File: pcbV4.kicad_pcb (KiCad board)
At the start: 4 copper layers, 61.1 x 30 mm, 55 parts, among them J3 GND, J4 GND, J5 VDD, J6 SWDCLK, J7 SWDIO, SW1 XDMK-12C01-25, U1 LSM6DSOXTR, U2 MAX30001CWV+T, U4 NPM1100-QDAA-R, U5 BS-08-B2AA020-R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

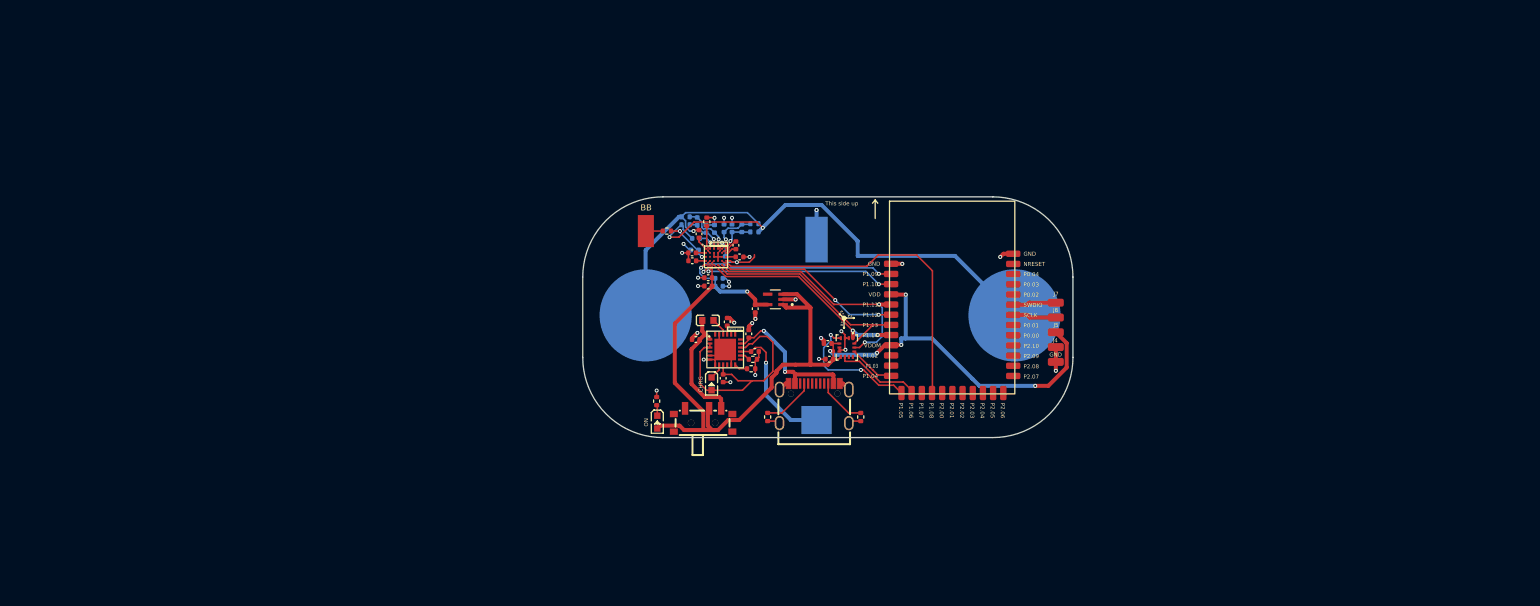
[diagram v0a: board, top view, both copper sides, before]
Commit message: Update pcbV4 KiCad design
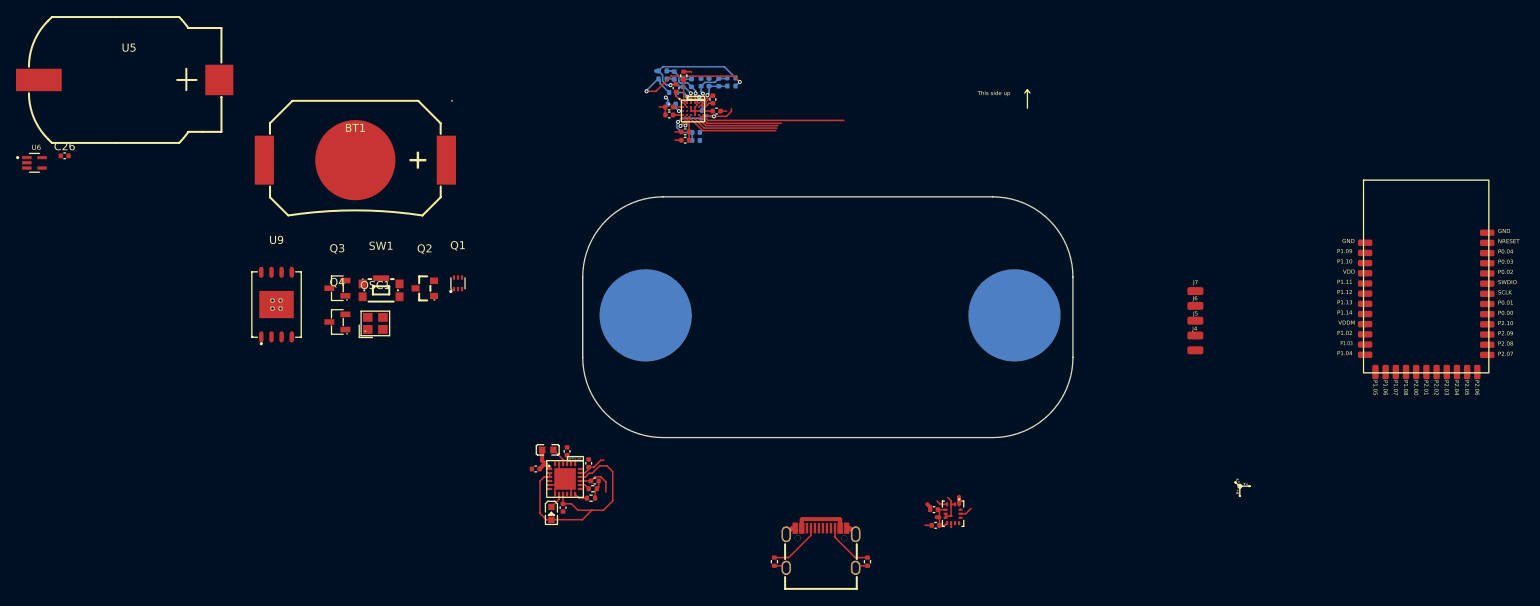
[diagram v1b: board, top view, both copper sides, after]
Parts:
- removed BB: Conn_01x01_Pin, Connector_Wire:SolderWirePad_1x01_SMD_5x10mm
- removed LED2: Blue light 0603, easyeda2kicad:LED0603-RD
- removed R11: 4k7, Resistor_SMD:R_0402_1005Metric
- removed R5: 200k, Resistor_SMD:R_0402_1005Metric
- added BT1: MY-2032-12, easyeda2kicad:BAT-SMD_MY-2032-12, F.Cu at (71.4, 81.6)
- added OSC1: SX2M32.768KM20F30TNN, easyeda2kicad:OSC-SMD_4P-L2.5-W2.0-BL, F.Cu at (73.9, 101.9)
- added Q1: DMC2400UV-7, easyeda2kicad:SOT-563_L1.6-W1.2-P0.50-LS1.6-BL, F.Cu at (84.2, 96.9)
- added Q2: AO3401A, easyeda2kicad:SOT-23_L2.9-W1.3-P1.90-LS2.4-BR, F.Cu at (80.0, 97.6)
- added Q3: MMBT3904-TP, easyeda2kicad:SOT-23-3_L2.9-W1.3-P1.90-LS2.4-BR, F.Cu at (69.1, 97.6)
- added Q4: MMBT3904-TP, easyeda2kicad:SOT-23-3_L2.9-W1.3-P1.90-LS2.4-BR, F.Cu at (69.1, 101.8)
- added U9: W25Q256JVEIQTR, easyeda2kicad:WSON-8_L8.0-W6.10-P1.27-BL-EP, F.Cu at (61.5, 99.6)
- C13: value C -> 10uF
- J3: value GND -> NRESET
- R3, R4: value 200k -> 200
- R9: value 1k5 -> 14k
- SW1: value XDMK-12C01-25 -> KMR221GLFS; footprint easyeda2kicad:SW-SMD_XDMK-12C01-25 -> easyeda2kicad:KEY-SMD_KMR2XXGXXX
- U5: moved to F.Cu
- moved U6 94.0 mm to (31.3, 81.9), turned to 0 degrees
- moved U5 91.2 mm to (43.1, 71.6), turned to 0 degrees
- moved C26 88.2 mm to (35.1, 81.0), turned to 0 degrees
- moved U3 59.2 mm to (197.1, 84.1)
- moved SW1 43.4 mm to (74.6, 97.5), turned to 0 degrees
- moved C21 25.7 mm to (93.9, 120.1)
- moved C22 25.7 mm to (100.5, 119.4)
- moved C24 25.7 mm to (101.2, 121.6)
- moved C23 25.7 mm to (97.8, 117.9)
- moved C25 25.7 mm to (97.3, 124.9)
- moved L1 25.7 mm to (95.4, 117.7)
- moved LED1 25.7 mm to (95.8, 125.6)
- moved R10 25.7 mm to (101.0, 122.6)
- moved R9 25.7 mm to (100.8, 123.7)
- moved U4 25.7 mm to (97.5, 121.3)
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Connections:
- C1 pad 2: bat- -> GND
- C10 pad 2: bat- -> GND
- C12 pad 2: bat- -> GND
- C13 pad 2: bat- -> GND
- C14 pad 2: bat- -> GND
- C15 pad 2: bat- -> GND
- C16 pad 2: bat- -> GND
- C17 pad 2: bat- -> GND
- C18 pad 2: bat- -> GND
- C19 pad 2: bat- -> GND
- C20 pad 2: bat- -> GND
- C21 pad 1: VOUT -> npm_out
- C21 pad 2: bat- -> GND
- C22 pad 1: bat- -> GND
- C23 pad 2: bat- -> GND
- C24 pad 2: bat- -> GND
- C25 pad 2: bat- -> GND
- C26 pad 2: bat- -> GND
- C4 pad 2: bat- -> GND
- C5 pad 1: bat- -> GND
- C6 pad 2: bat- -> GND
- C7 pad 1: bat- -> GND
- J3 pad 1: bat- -> NRESET
- J4 pad 1: bat- -> GND
- L1 pad 1: VOUT -> npm_out
- R10 pad 1: bat- -> GND
- R6 pad 2: bat- -> GND
- R7 pad 2: bat- -> GND
- R8 pad 2: bat- -> GND
- R9 pad 1: bat- -> GND
- SW1 pad 1: VOUT -> Net-(Q3-B)
- SW1 pad 2: VDD -> unconnected-(SW1-Pad2)
- SW1 pad 3: unconnected-(SW1-Pad3) -> Net-(Q4-C)
- SW1 pad 4: (no net) -> unconnected-(SW1-Pad4)
- SW1 pad 5: (no net) -> unconnected-(SW1-Pad5)
- U1 pad 2: bat- -> GND
- U1 pad 3: bat- -> GND
- U1 pad 6: bat- -> GND
- U1 pad 7: bat- -> GND
- U2 pad B3: bat- -> GND
- U2 pad B4: bat- -> GND
- U2 pad C3: bat- -> GND
- U2 pad C4: bat- -> GND
- U2 pad C5: bat- -> GND
- U2 pad D4: bat- -> GND
- U3 pad 1: bat- -> GND
- U3 pad 16: FCLK -> unconnected-(U3-P1.08-Pad16)
- U3 pad 36: bat- -> GND
- U4 pad 1: VOUT -> npm_out
- U4 pad 11: bat- -> GND
- U4 pad 23: bat- -> GND
- U4 pad 25: bat- -> GND
- U4 pad 5: bat- -> GND
- U4 pad 6: bat- -> SHPACT
- U4 pad 7: bat- -> GND
- U5 pad 2: bat- -> GND
- U6 pad 2: bat- -> GND
- USBC1 pad 1: bat- -> GND
- USBC1 pad 2: bat- -> GND
- USBC1 pad 3: bat- -> GND
- USBC1 pad 4: bat- -> GND
- USBC1 pad A1B12: bat- -> GND
- USBC1 pad B1A12: bat- -> GND
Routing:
- net VDD: track 120.9 -> 7.89 mm, vias 5 -> 0
- net bat-: track 60.3 -> 0.00 mm, vias 28 -> 0
- net ECGN: track 58.0 -> 17.9 mm
- net GND: track 0.00 -> 36.3 mm, vias 0 -> 2
- net FCLK: track 43.2 -> 18.3 mm
- net INT2B_MAX30001: track 24.4 -> 0.90 mm, vias 2 -> 1
- net INTB_MAX30001: track 25.7 -> 2.92 mm, vias 2 -> 1
- net SCLK: track 31.4 -> 11.8 mm, vias 2 -> 0
- net MOSI: track 28.3 -> 10.7 mm
- net INT1_LSM: track 16.7 -> 1.42 mm, vias 2 -> 0
- net VOUT: track 15.3 -> 0.00 mm
- net MISO: track 26.7 -> 12.1 mm, vias 2 -> 0
- net ECGP: track 28.1 -> 14.1 mm
- net CS_MAX: track 23.2 -> 9.98 mm, vias 2 -> 0
- net bat+: track 16.6 -> 4.92 mm, vias 1 -> 0
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- added copper zone on In1.Cu, net GND
- added copper zone on In2.Cu, net GND
- removed copper zone on In1.Cu, net bat-
- removed copper zone on In2.Cu, net bat-
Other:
- board text removed: "CHRG"
- board text removed: "ON"

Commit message: Update pcbV4 KiCad design
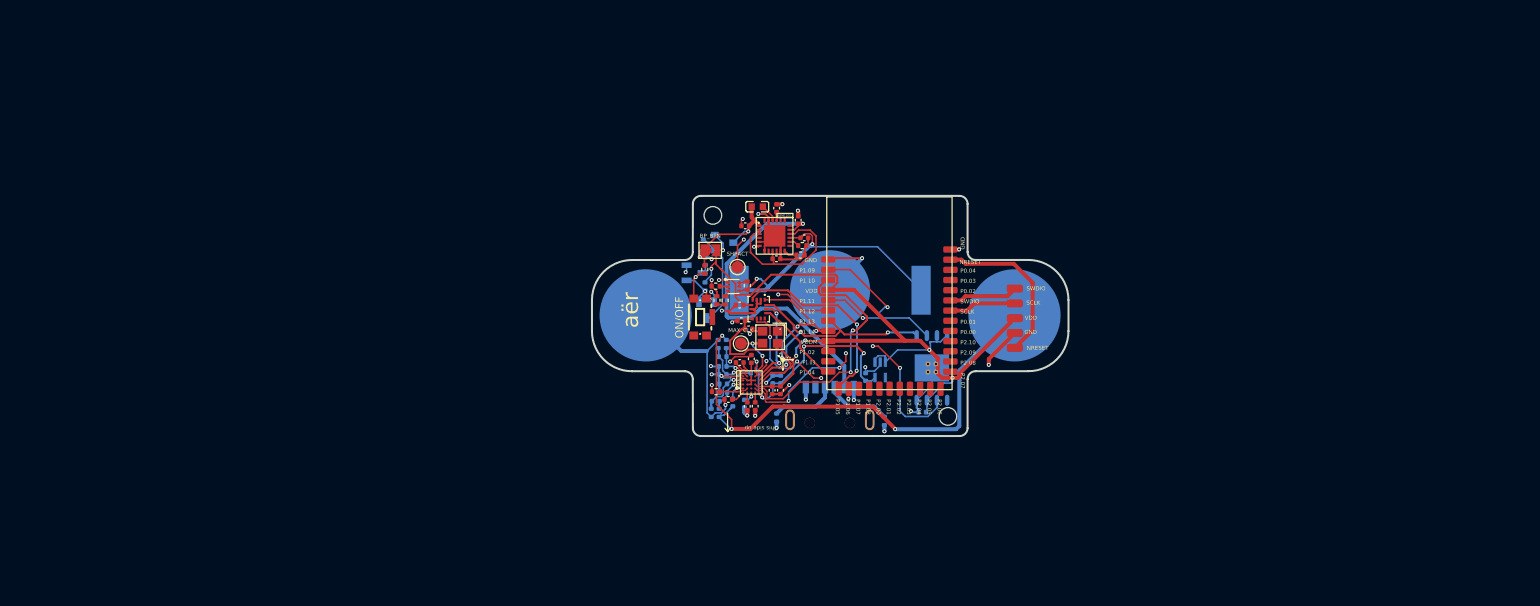
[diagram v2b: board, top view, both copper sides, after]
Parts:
- removed LED1: Blue light 0603, easyeda2kicad:LED0603-RD
- removed SW1: KMR221GLFS, easyeda2kicad:KEY-SMD_KMR2XXGXXX
- removed U5: BS-08-B2AA020-R, easyeda2kicad:BAT-SMD_BS-08-B2AA016
- removed USBC1: TYPE-C-31-M-12, easyeda2kicad:USB-C_SMD-TYPE-C-31-M-12_1
- added BP_BTN: SolderJumper_2_Open, Jumper:SolderJumper-2_P1.3mm_Open_TrianglePad1.0x1.5mm, F.Cu at (115.6, 92.8)
- added C28: 0.01uF, Capacitor_SMD:C_0402_1005Metric, F.Cu at (120.4, 102.6)
- added C29: 22uF, Capacitor_SMD:C_0402_1005Metric, B.Cu at (115.0, 94.2)
- added C30: 100nF, Capacitor_SMD:C_0402_1005Metric, B.Cu at (142.1, 113.0)
- added H1: MountingHole, MountingHole:MountingHole_2.2mm_M2, F.Cu at (145.3, 113.5)
- added H2: MountingHole, MountingHole:MountingHole_2.2mm_M2, F.Cu at (116.0, 88.5)
- added MAX_CLK: TestPoint, TestPoint:TestPoint_Pad_D1.5mm, F.Cu at (119.5, 104.5)
- added ON/OFF: KMR221GLFS, easyeda2kicad:KEY-SMD_KMR2XXGXXX, F.Cu at (114.7, 101.2)
- added R11: 1M, Resistor_SMD:R_0402_1005Metric, F.Cu at (116.3, 97.3)
- added R12: 1M5, Resistor_SMD:R_0402_1005Metric, F.Cu at (117.5, 99.1)
- added R13: 220k, Resistor_SMD:R_0402_1005Metric, F.Cu at (116.5, 99.1)
- added R14: 1M, Resistor_SMD:R_0402_1005Metric, F.Cu at (120.2, 97.2)
- added R15: 100k, Resistor_SMD:R_0402_1005Metric, B.Cu at (114.8, 92.0)
- added R16: 100k, Resistor_SMD:R_0402_1005Metric, B.Cu at (115.0, 97.3)
- added R17: 660k, Resistor_SMD:R_0402_1005Metric, F.Cu at (114.9, 95.2)
- added SHPACT: TestPoint, TestPoint:TestPoint_Pad_D1.5mm, F.Cu at (119.0, 94.9)
- added USB2: USBC-0032IPX8-00, easyeda2kicad:TYPE-C-USB-SMD_USBC-0032IPX8-00, B.Cu at (130.5, 111.9)
- BT1, C26, Q2, Q3, Q4, R7, R8, U6, U9: moved to B.Cu
- moved U6 108.6 mm to (136.8, 107.7), turned to -90 degrees
- moved C26 103.6 mm to (135.0, 108.6), turned to 90 degrees
- moved U9 82.1 mm to (143.3, 107.5), turned to 180 degrees
- moved U3 67.0 mm to (130.2, 86.2)
- moved BT1 61.4 mm to (130.6, 97.8)
- moved OSC1 49.3 mm to (123.1, 103.7), turned to 180 degrees
- moved Q3 46.1 mm to (115.2, 100.3), turned to 90 degrees
- moved Q4 45.0 mm to (113.7, 95.6), turned to 180 degrees
- moved R3 43.1 mm to (115.7, 113.1), turned to 90 degrees
- moved R4 42.2 mm to (116.7, 113.1), turned to 90 degrees
- moved C3 41.0 mm to (116.3, 111.6), turned to 0 degrees
- moved C25 40.9 mm to (123.9, 93.9), turned to 0 degrees
- moved C21 40.0 mm to (120.0, 89.8)
- moved C22 40.0 mm to (126.6, 89.1)
- moved C24 40.0 mm to (127.4, 91.3)
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- renumbered J4 to GND, J6 to SCLK, J7 to SWDIO, J5 to VDD
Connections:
- R7 pad 1: Net-(USBC1-CC2) -> GND
- R7 pad 2: GND -> Net-(USB2-CC1)
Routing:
- net VDD: track 7.89 -> 122.7 mm, vias 0 -> 6
- net GND: track 36.3 -> 108.3 mm, vias 2 -> 30
- net ECGN: track 17.9 -> 65.9 mm, vias 2 -> 3
- net MISO: track 12.1 -> 48.5 mm, vias 0 -> 5
- net bat+: track 4.92 -> 37.2 mm, vias 0 -> 2
- net INTB_MAX30001: track 2.92 -> 34.8 mm, vias 1 -> 4
- net VBUS: track 10.7 -> 41.2 mm, vias 0 -> 1
- net INT2B_MAX30001: track 0.90 -> 31.3 mm, vias 1 -> 2
- net SCLK: track 11.8 -> 36.1 mm, vias 0 -> 3
- net INT1_LSM: track 1.42 -> 24.6 mm, vias 0 -> 2
- net MOSI: track 10.7 -> 32.4 mm, vias 0 -> 3
- net NRESET: track 0.00 -> 20.5 mm
- net INT2_LSM: track 0.57 -> 20.2 mm, vias 0 -> 4
- net VCC: track 13.4 -> 29.9 mm, vias 2 -> 4
- net npm_out: track 3.68 -> 18.2 mm, vias 0 -> 2
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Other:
- board size 61.1 x 30 mm -> 59.4 x 30 mm
- board text added: "aër"

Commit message: Update pcbV4 KiCad design
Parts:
- removed BP_BTN: SolderJumper_2_Open, Jumper:SolderJumper-2_P1.3mm_Open_TrianglePad1.0x1.5mm
- removed C28: 0.01uF, Capacitor_SMD:C_0402_1005Metric
- removed C29: 22uF, Capacitor_SMD:C_0402_1005Metric
- removed OSC1: SX2M32.768KM20F30TNN, easyeda2kicad:OSC-SMD_4P-L2.5-W2.0-BL
- removed Q2: AO3401A, easyeda2kicad:SOT-23_L2.9-W1.3-P1.90-LS2.4-BR
- removed Q3, Q4: MMBT3904-TP, easyeda2kicad:SOT-23-3_L2.9-W1.3-P1.90-LS2.4-BR
- removed R15, R16: 100k, Resistor_SMD:R_0402_1005Metric
- removed R17: 660k, Resistor_SMD:R_0402_1005Metric
- added G***: LOGO, easyeda2kicad:aer_logo, F.Cu at (107.2, 101.2)
- added LED1: 19-237/R6GHBHC-A07/2T, easyeda2kicad:LED-ARRAY-SMD_4P-L1.6-W1.6-BL-CW, F.Cu at (125.8, 96.3)
- added MISO: TestPoint, TestPoint:TestPoint_Pad_D1.5mm, F.Cu at (138.6, 112.8)
- added MOSI: TestPoint, TestPoint:TestPoint_Pad_D1.5mm, F.Cu at (141.5, 112.9)
- added R18: 1k, Resistor_SMD:R_0402_1005Metric, F.Cu at (123.9, 96.3)
- added R19: 1k, Resistor_SMD:R_0402_1005Metric, F.Cu at (128.1, 95.8)
- added R5: 1k, Resistor_SMD:R_0402_1005Metric, F.Cu at (128.1, 96.8)
- moved FCLK 2.10 mm to (121.4, 103.6)
- renumbered ON/OFF to BTN, MAX_CLK to FCLK
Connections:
- BTN pad 1: Net-(Q3-B) -> NRF_BUTTON
- BTN pad 3: Net-(Q4-C) -> GND
- C21 pad 1: npm_out -> VDD
- L1 pad 1: npm_out -> VDD
- U3 pad 10: SDA -> unconnected-(U3-P1.02-Pad10)
- U3 pad 11: SCL -> unconnected-(U3-P1.03-Pad11)
- U3 pad 15: unconnected-(U3-P1.07-Pad15) -> BAT_MON
- U3 pad 16: unconnected-(U3-P1.08-Pad16) -> NRF_BUTTON
- U3 pad 22: unconnected-(U3-P2.05-Pad22) -> W25_CS
- U3 pad 25: unconnected-(U3-P2.08-Pad25) -> BAT_MON_EN
- U3 pad 27: unconnected-(U3-P2.10-Pad27) -> CHG
- U3 pad 28: unconnected-(U3-P0.00-Pad28) -> LED_RED_DRAIN
- U3 pad 29: unconnected-(U3-P0.01-Pad29) -> LED_GREEN_DRAIN
- U3 pad 32: unconnected-(U3-P0.02-Pad32) -> LED_BLUE_DRAIN
- U3 pad 34: unconnected-(U3-P0.04-Pad34) -> FCLK
- U4 pad 1: npm_out -> VDD
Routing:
- net BAT_MON_EN: track 1.02 -> 47.2 mm, vias 0 -> 4
- net BAT_MON: track 1.02 -> 41.8 mm, vias 0 -> 2
- net NRF_BUTTON: track 0.00 -> 38.8 mm, vias 0 -> 2
- net CHG: track 0.00 -> 37.0 mm, vias 0 -> 4
- net FCLK: track 8.93 -> 40.9 mm, vias 2 -> 5
- net LED_GREEN_DRAIN: track 0.00 -> 31.4 mm, vias 0 -> 2
- net LED_RED_DRAIN: track 0.00 -> 21.9 mm, vias 0 -> 2
- net LED_BLUE_DRAIN: track 0.00 -> 21.0 mm
- net npm_out: track 18.2 -> 0.00 mm, vias 2 -> 0
- net Net-(Q2-G): track 11.9 -> 0.00 mm
- net MOSI: track 32.4 -> 42.7 mm, vias 3 -> 4
- net VDD: track 122.7 -> 114.6 mm, vias 6 -> 4
- net Net-(Q4-C): track 6.30 -> 0.00 mm, vias 1 -> 0
- net Net-(Q3-B): track 5.62 -> 0.00 mm, vias 1 -> 0
- net GND: track 108.3 -> 104.0 mm, vias 30 -> 26
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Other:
- board text removed: "aër"
